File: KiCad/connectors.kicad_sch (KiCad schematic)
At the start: 27 parts, among them J2 USB-C, J3 Header_FFC_1.0mm_06, J4 Header_50mil_2x07, J5 Header_FFC_1.0mm_10, J6 Header_FFC_1.0mm_10, J7 JST_PH_2.0mm_1x03

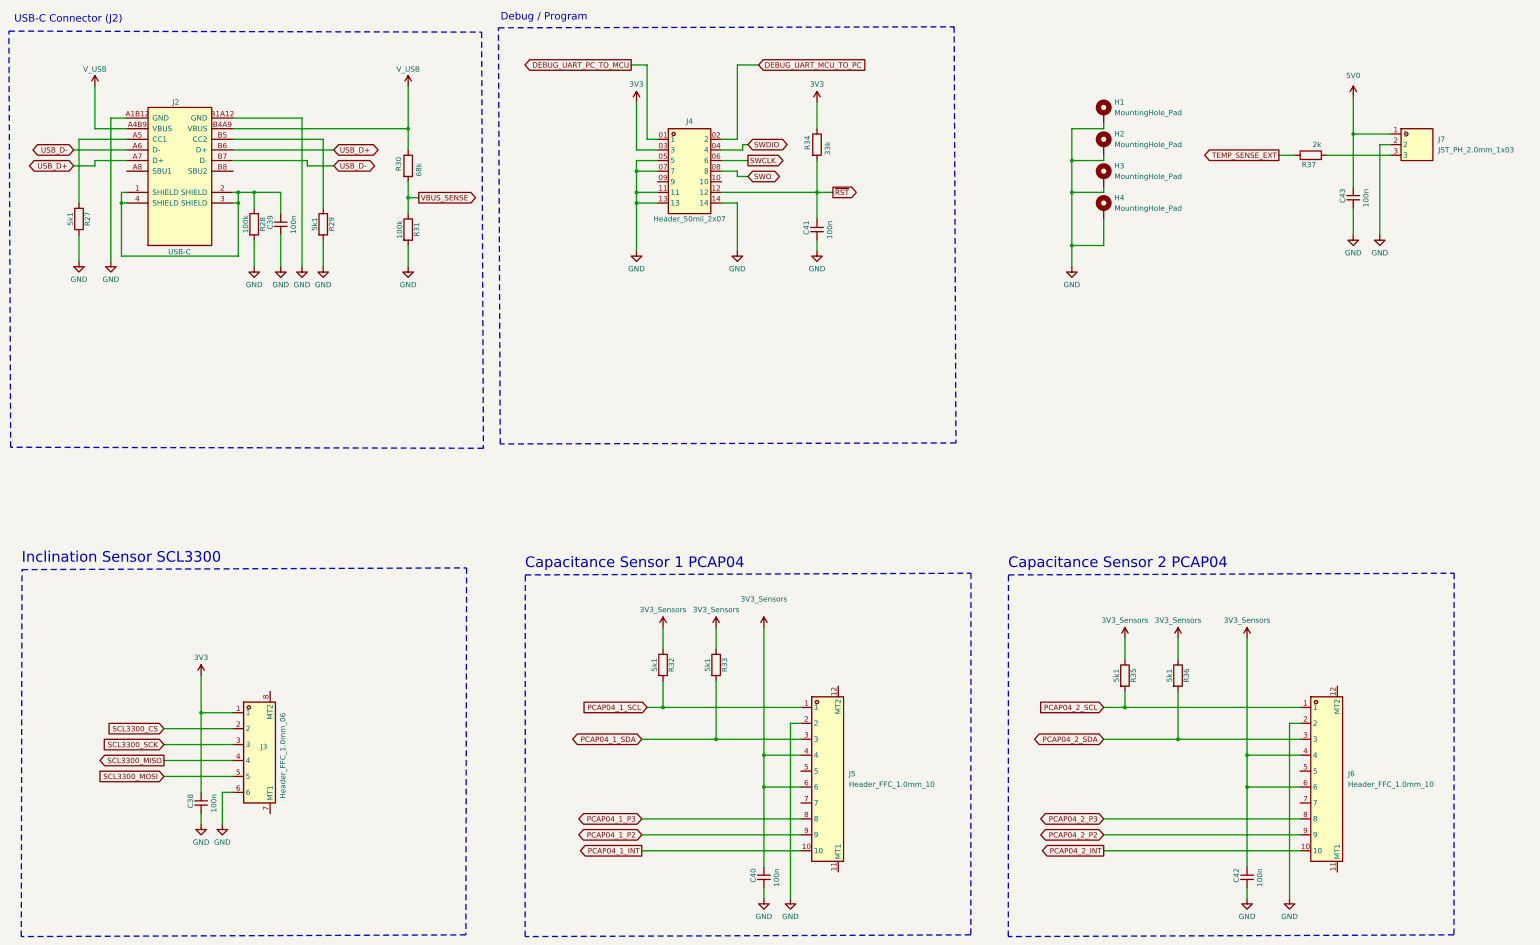
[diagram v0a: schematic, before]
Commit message: Capacitors changed to specific symbols, board layout not yet complete
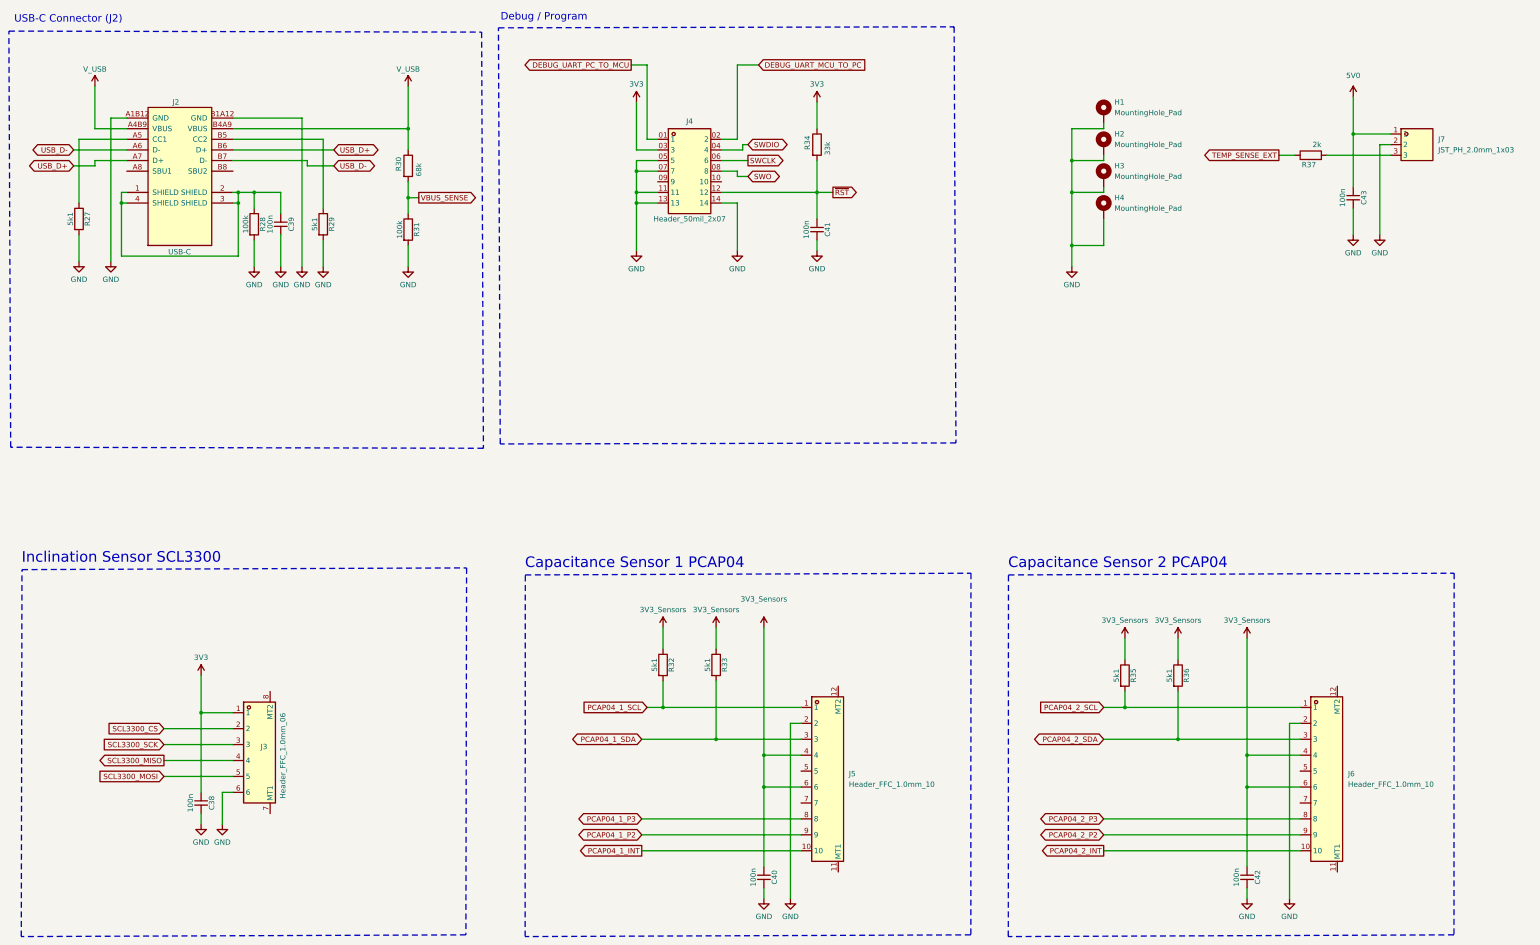
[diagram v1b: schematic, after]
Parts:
- C38, C39, C40, C41, C42, C43: symbol sldrnrd:Capacitor/C_0603 -> sldrnrd:Capacitor/C0603_100n; Dielectric (none) -> X7R; LCSC (none) -> C14663; MPN (none) -> CC0603KRX7R9BB104; Manufacturer (none) -> Yageo; Voltage (none) -> 50V

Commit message: Symbols and board updated to match library
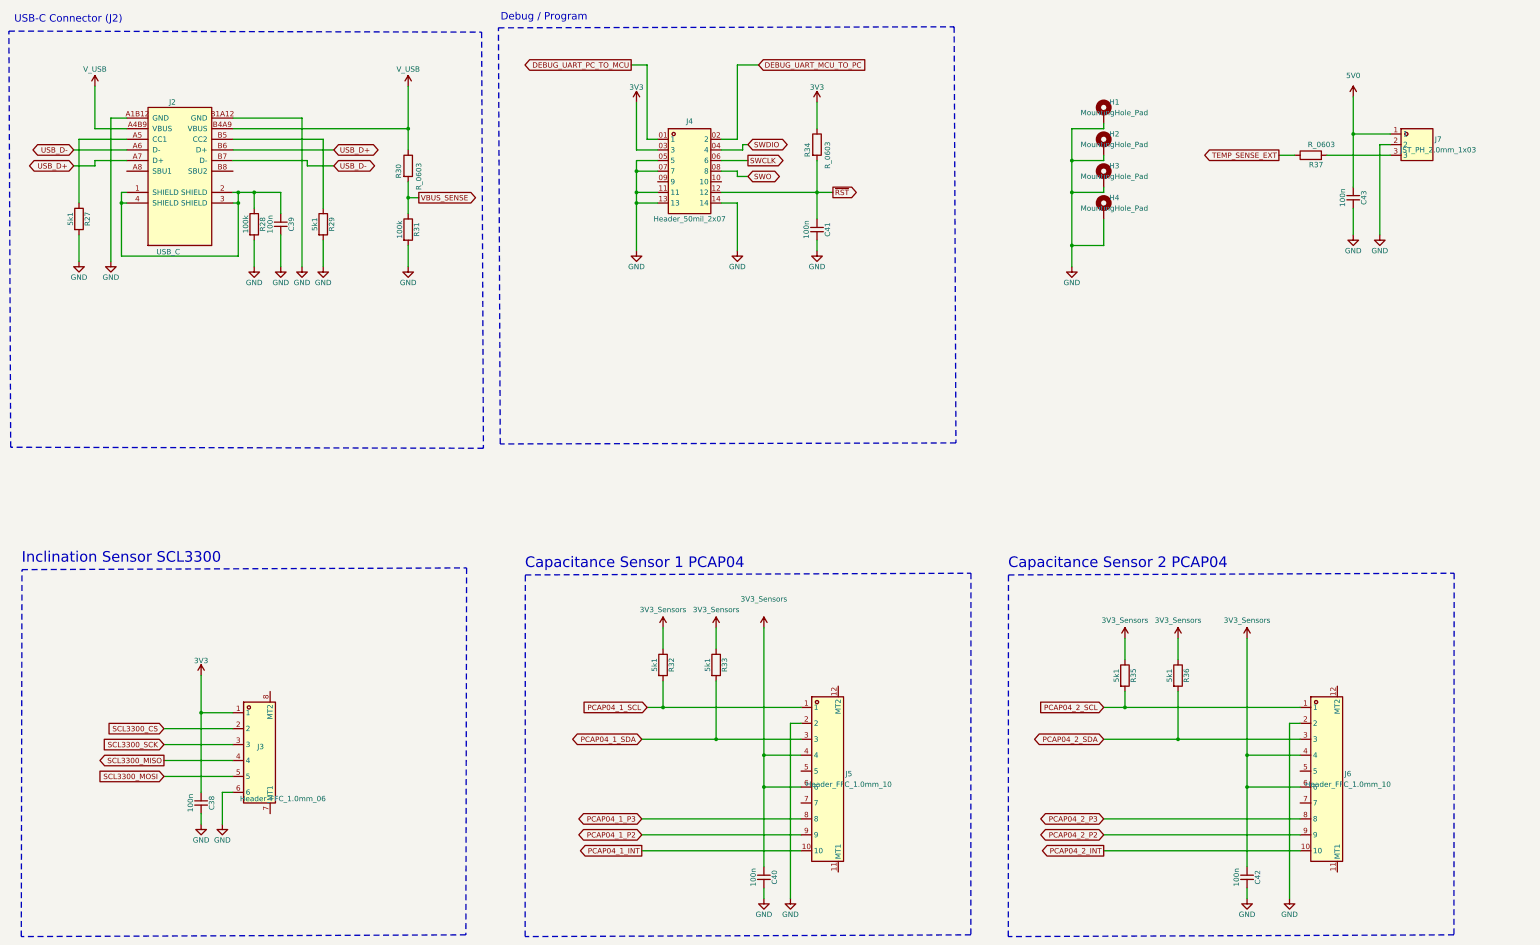
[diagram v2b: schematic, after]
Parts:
- J2: value USB-C -> USB_C
- R30: value 68k -> R_0603
- R34: value 33k -> R_0603
- R37: value 2k -> R_0603

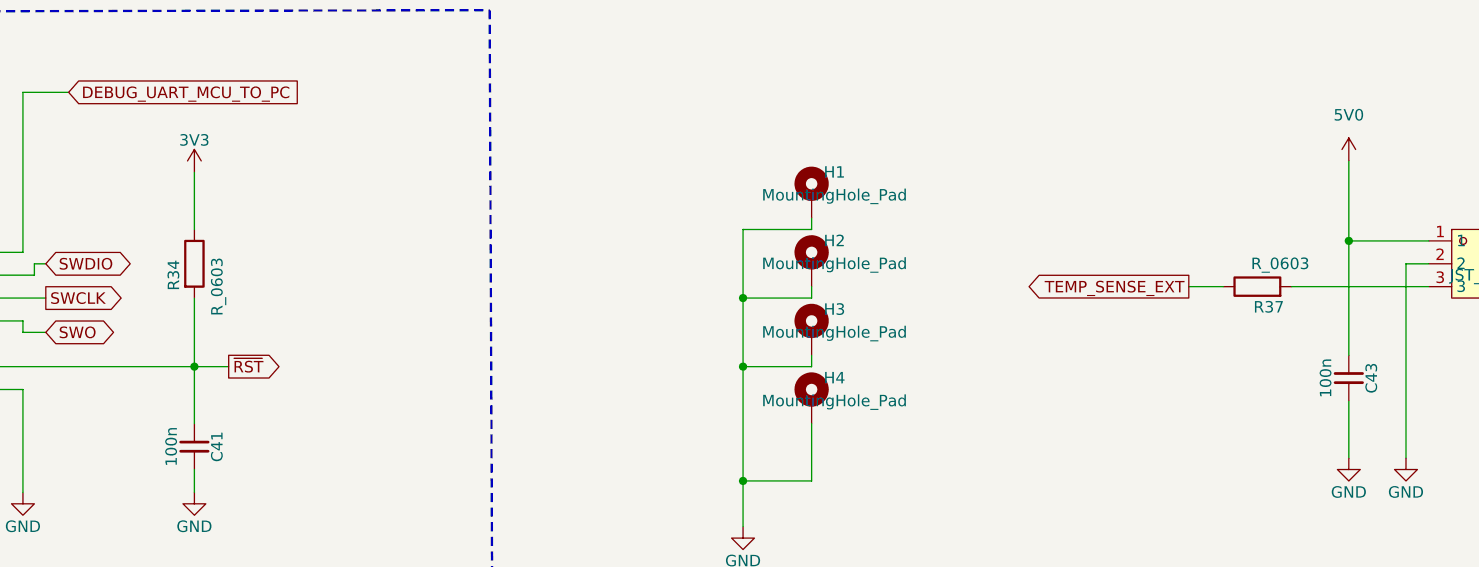
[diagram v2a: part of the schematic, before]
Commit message: Remaining resistors and capacitors replaced by specific value components
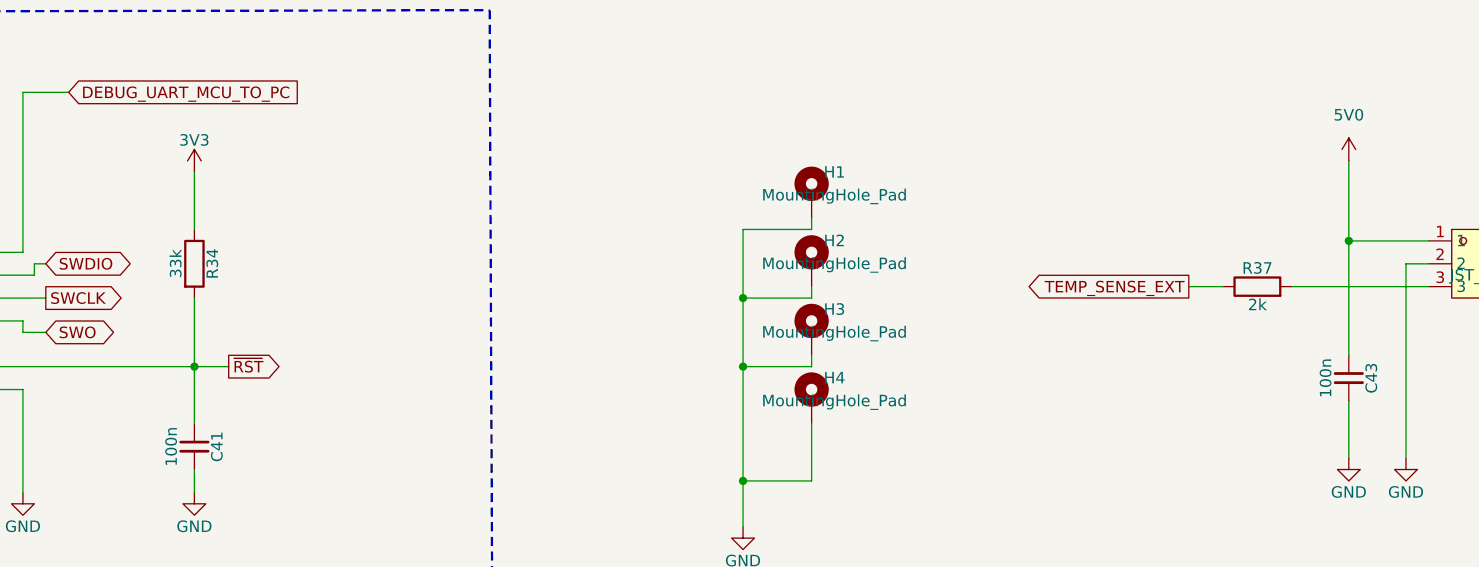
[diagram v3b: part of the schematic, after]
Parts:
- J4: LCSC (none) -> C5563894
- R34: value R_0603 -> 33k; symbol sldrnrd:Resistor/R_0603 -> sldrnrd:Resistor/R0603_33k; LCSC (none) -> C4216; MPN (none) -> 0603WAF3302T5E; Manufacturer (none) -> Uni-Royal
- R37: value R_0603 -> 2k; symbol sldrnrd:Resistor/R_0603 -> sldrnrd:Resistor/R0603_2k; LCSC (none) -> C22975; MPN (none) -> 0603WAF2001T5E; Manufacturer (none) -> Uni-Royal
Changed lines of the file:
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@@
 	)
 	(symbol
-		(lib_id "sldrnrd:Resistor/R_0603")
+		(lib_id "sldrnrd:Resistor/R0603_33k")
 		(at 217.17 53.34 0)
 		(unit 1)
@@
 		(dnp no)
 		(property "Reference" "R34"
-			(at 214.884 54.61 90)
-			(show_name no)
-			(do_not_autoplace no)
-			(effects
-				(font
-					(size 1.27 1.27)
-				)
-			)
-		)
-		(property "Value" "R_0603"
-			(at 219.71 55.88 90)
+			(at 219.202 53.34 90)
+			(show_name no)
+			(do_not_autoplace no)
+			(effects
+				(font
+					(size 1.27 1.27)
+				)
+			)
+		)
+		(property "Value" "33k"
+			(at 215.138 53.34 90)
 			(show_name no)
 			(do_not_autoplace no)
@@
 			)
 		)
-		(property "Description" "Resistor"
+		(property "Description" "33k Resistor, 0603, 1%, 75V, 100mW"
+			(at 217.17 53.34 0)
+			(hide yes)
+			(show_name no)
+			(do_not_autoplace no)
+			(effects
+				(font
+					(size 1.27 1.27)
+				)
+			)
+		)
+		(property "Manufacturer" "Uni-Royal"
+			(at 217.17 53.34 0)
+			(hide yes)
+			(show_name no)
+			(do_not_autoplace no)
+			(effects
+				(font
+					(size 1.27 1.27)
+				)
+			)
+		)
+		(property "MPN" "0603WAF3302T5E"
+			(at 217.17 53.34 0)
+			(hide yes)
+			(show_name no)
+			(do_not_autoplace no)
+			(effects
+				(font
+					(size 1.27 1.27)
+				)
+			)
+		)
+		(property "LCSC" "C4216"
 			(at 217.17 53.34 0)
 			(hide yes)
@@
 	)
 	(symbol
-		(lib_id "sldrnrd:Resistor/R_0603")
+		(lib_id "sldrnrd:Resistor/R0603_2k")
 		(at 335.28 55.88 90)
 		(unit 1)
@@
 		(dnp no)
 		(property "Reference" "R37"
-			(at 336.55 58.166 90)
-			(show_name no)
-			(do_not_autoplace no)
-			(effects
-				(font
-					(size 1.27 1.27)
-				)
-			)
-		)
-		(property "Value" "R_0603"
-			(at 337.82 53.34 90)
+			(at 335.28 53.848 90)
+			(show_name no)
+			(do_not_autoplace no)
+			(effects
+				(font
+					(size 1.27 1.27)
+				)
+			)
+		)
+		(property "Value" "2k"
+			(at 335.28 57.912 90)
 			(show_name no)
 			(do_not_autoplace no)
@@
 			)
 		)
-		(property "Description" "Resistor"
+		(property "Description" "2k Resistor, 0603, 1%, 75V, 100mW"
+			(at 335.28 55.88 0)
+			(hide yes)
+			(show_name no)
+			(do_not_autoplace no)
+			(effects
+				(font
+					(size 1.27 1.27)
+				)
+			)
+		)
+		(property "Manufacturer" "Uni-Royal"
+			(at 335.28 55.88 0)
+			(hide yes)
+			(show_name no)
+			(do_not_autoplace no)
+			(effects
+				(font
+					(size 1.27 1.27)
+				)
+			)
+		)
+		(property "MPN" "0603WAF2001T5E"
+			(at 335.28 55.88 0)
+			(hide yes)
+			(show_name no)
+			(do_not_autoplace no)
+			(effects
+				(font
+					(size 1.27 1.27)
+				)
+			)
+		)
+		(property "LCSC" "C22975"
 			(at 335.28 55.88 0)
 			(hide yes)
@@
 			(at 186.69 59.69 0)
 			(hide yes)
+			(show_name no)
+			(do_not_autoplace no)
+			(effects
+				(font
+					(size 1.27 1.27)
+				)
+			)
+		)
+		(property "LCSC" "C5563894"
+			(at 186.69 59.69 0)
+			(hide yes)

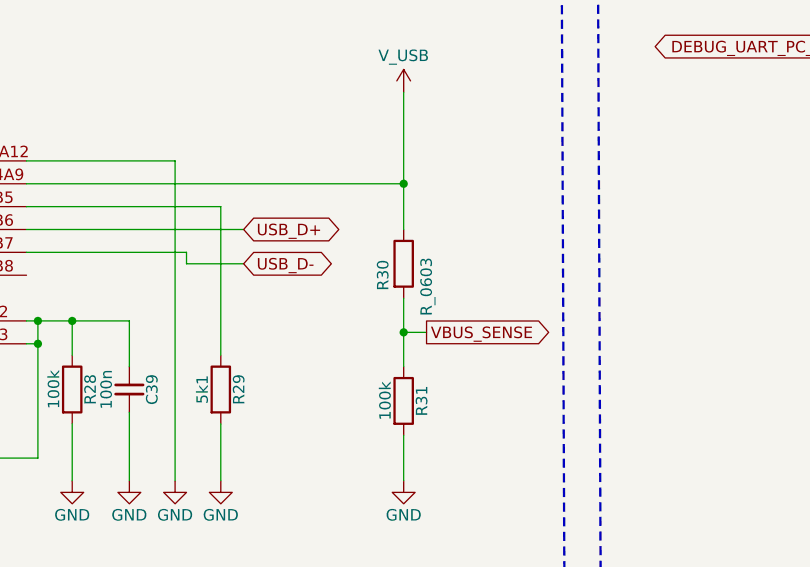
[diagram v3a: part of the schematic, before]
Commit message: R30 fixed as well
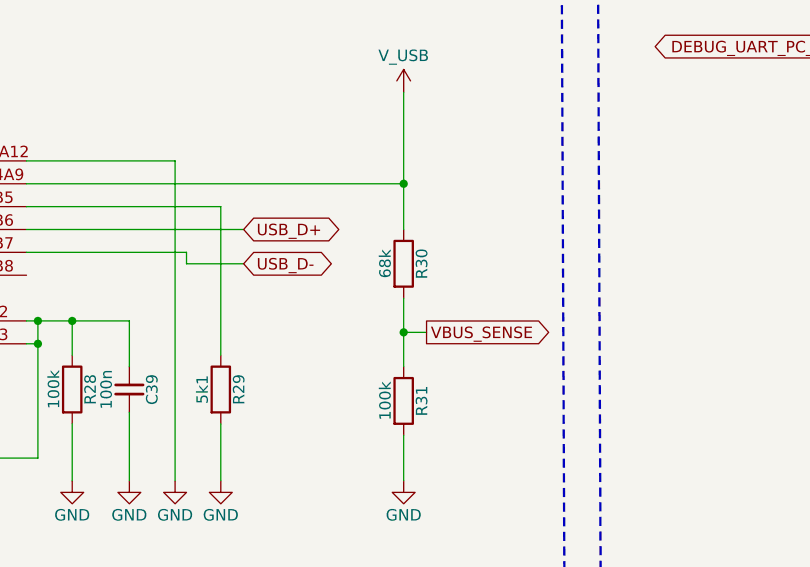
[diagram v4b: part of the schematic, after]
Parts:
- R30: value R_0603 -> 68k; symbol sldrnrd:Resistor/R_0603 -> sldrnrd:Resistor/R0603_68k; LCSC (none) -> C23231; MPN (none) -> 0603WAF6802T5E; Manufacturer (none) -> Uni-Royal
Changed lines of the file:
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@@
 	)
 	(symbol
-		(lib_id "sldrnrd:Resistor/R_0603")
+		(lib_id "sldrnrd:Resistor/R0603_68k")
 		(at 119.38 58.42 0)
 		(unit 1)
@@
 		(dnp no)
 		(property "Reference" "R30"
-			(at 117.094 59.69 90)
+			(at 121.412 58.42 90)
 			(show_name no)
 			(do_not_autoplace no)
@@
 			)
 		)
-		(property "Value" "R_0603"
-			(at 121.92 60.96 90)
+		(property "Value" "68k"
+			(at 117.348 58.42 90)
 			(show_name no)
 			(do_not_autoplace no)
@@
 			)
 		)
-		(property "Description" "Resistor"
+		(property "Description" "68k Resistor, 0603, 1%, 75V, 100mW"
 			(at 119.38 58.42 0)
 			(hide yes)
+			(show_name no)
+			(do_not_autoplace no)
+			(effects
+				(font
+					(size 1.27 1.27)
+				)
+			)
+		)
+		(property "Manufacturer" "Uni-Royal"
+			(at 119.38 58.42 0)
+			(hide yes)
+			(show_name no)
+			(do_not_autoplace no)
+			(effects
+				(font
+					(size 1.27 1.27)
+				)
+			)
+		)
+		(property "MPN" "0603WAF6802T5E"
+			(at 119.38 58.42 0)
+			(hide yes)
+			(show_name no)
+			(do_not_autoplace no)
+			(effects
+				(font
+					(size 1.27 1.27)
+				)
+			)
+		)
+		(property "LCSC" "C23231"
+			(at 119.38 58.42 0)
+			(hide yes)
